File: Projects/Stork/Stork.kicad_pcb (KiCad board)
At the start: 4 copper layers, 200 x 100 mm, 567 parts, among them J1 Conn_01x05, J10 Conn_01x05, J11 Conn_01x05, J12 Conn_01x05, J13 Conn_01x05, J14 Conn_01x05, J15 Conn_01x05, J16 Conn_01x05, J17 Conn_01x05, J18 Conn_01x05, J19 Conn_01x05, J2 Conn_01x05, J20 Conn_01x05, J21 Conn_01x05, J22 Conn_01x05, J23 Conn_01x05, J24 Conn_01x05, J25 Conn_02x03_Odd_Even, J26 Conn_01x03_Male, J27 Screw_Terminal_01x02, J28 Conn_01x03_Male, J29 Conn_01x03_Male, J3 Conn_01x05, J30 Conn_01x03_Male, J4 Conn_01x05, J5 Conn_01x05, J6 Conn_01x05, J7 Conn_01x05, J8 Conn_01x05, J9 Conn_01x05, U1 AD7991YRJZ-1500RL7, U10 AD8608ARZ-SOIC127P600X175-14N, U11 AD7991YRJZ-1500RL7, U12 AD8608ARZ-SOIC127P600X175-14N, U13 AD7991YRJZ-1500RL7, U14 AD8608ARZ-SOIC127P600X175-14N, U15 AD7991YRJZ-1500RL7, U16 AD8608ARZ-SOIC127P600X175-14N, U17 AD7991YRJZ-1500RL7, U18 AD8608ARZ-SOIC127P600X175-14N, U19 AD7991YRJZ-1500RL7, U2 AD8608ARZ-SOIC127P600X175-14N, U20 AD8608ARZ-SOIC127P600X175-14N, U21 AD7991YRJZ-1500RL7, U22 AD8608ARZ-SOIC127P600X175-14N, U23 AD7991YRJZ-1500RL7, U24 AD8608ARZ-SOIC127P600X175-14N, U25 AD7991YRJZ-1500RL7, U26 AD8608ARZ-SOIC127P600X175-14N, U27 AD7991YRJZ-1500RL7, U28 AD8608ARZ-SOIC127P600X175-14N, U29 AD7991YRJZ-1500RL7, U3 AD7991YRJZ-1500RL7, U30 AD8608ARZ-SOIC127P600X175-14N, U31 AD7991YRJZ-1500RL7, U32 AD8608ARZ-SOIC127P600X175-14N, U33 Digilent-CoraZ7, U34 AD7991YRJZ-1500RL7, U35 AD8608ARZ-SOIC127P600X175-14N, U36 AD7991YRJZ-1500RL7, U37 AD8608ARZ-SOIC127P600X175-14N, U38 AD7991YRJZ-1500RL7, U39 AD8608ARZ-SOIC127P600X175-14N, U4 AD8608ARZ-SOIC127P600X175-14N, U40 AD7991YRJZ-1500RL7, U41 AD8608ARZ-SOIC127P600X175-14N, U42 AD7991YRJZ-1500RL7, U43 AD8608ARZ-SOIC127P600X175-14N, U44 AD7991YRJZ-1500RL7, U45 AD8608ARZ-SOIC127P600X175-14N, U46 AD7991YRJZ-1500RL7, U47 AD8608ARZ-SOIC127P600X175-14N, U48 AD7991YRJZ-1500RL7, U49 AD8608ARZ-SOIC127P600X175-14N, U5 AD7991YRJZ-1500RL7, U50 TPS79330-EP, U51 TPS73150DBV, U6 AD8608ARZ-SOIC127P600X175-14N, U7 AD7991YRJZ-1500RL7, U8 AD8608ARZ-SOIC127P600X175-14N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

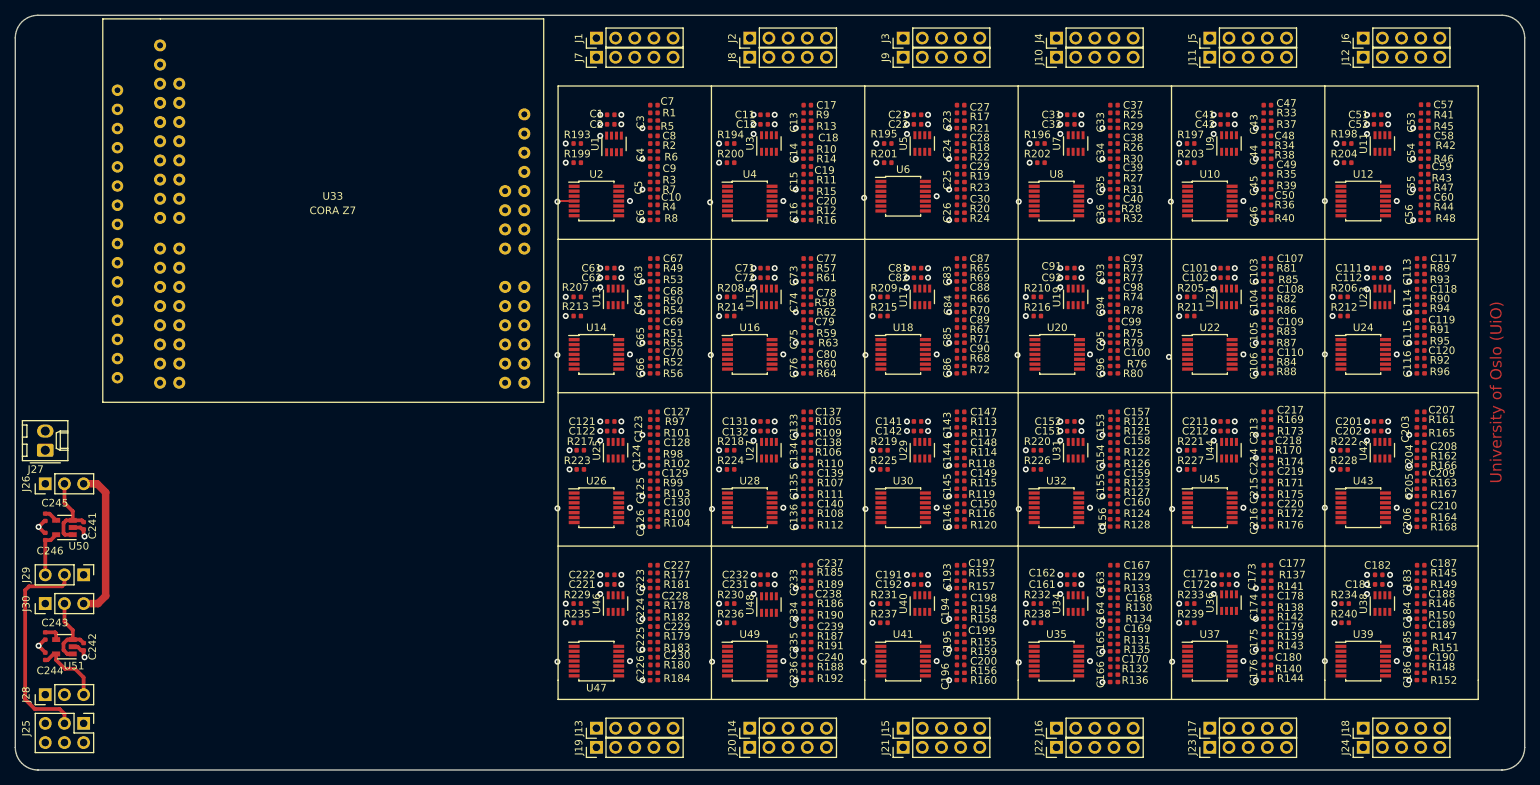
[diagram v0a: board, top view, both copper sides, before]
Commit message: changed position of cora z7 to be at center with cutout to give headroom for ethernet and powerjack
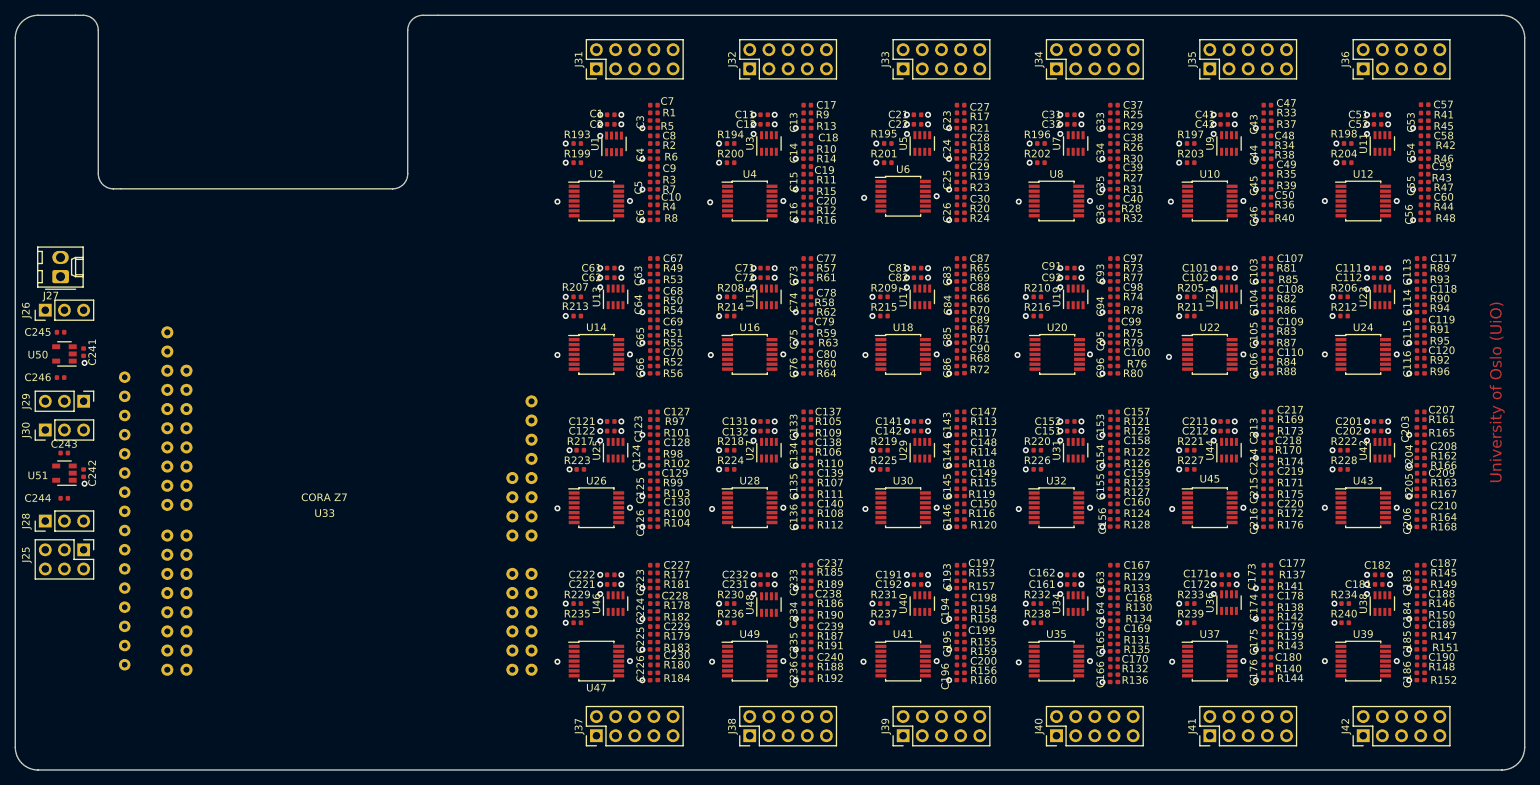
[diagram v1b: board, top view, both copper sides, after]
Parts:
- removed J1, J10, J11, J12, J13, J14, J15, J16, J17, J18, J19, J2, J20, J21, J22, J23, J24, J3, J4, J5, J6, J7, J8, J9: Conn_01x05, Connector_PinHeader_2.54mm:PinHeader_1x05_P2.54mm_Vertical
- added J31: Conn_02x05_Top_Bottom, Connector_PinHeader_2.54mm:PinHeader_2x05_P2.54mm_Vertical, F.Cu at (127.0, 37.1)
- added J32: Conn_02x05_Top_Bottom, Connector_PinHeader_2.54mm:PinHeader_2x05_P2.54mm_Vertical, F.Cu at (147.3, 37.1)
- added J33: Conn_02x05_Top_Bottom, Connector_PinHeader_2.54mm:PinHeader_2x05_P2.54mm_Vertical, F.Cu at (167.6, 37.1)
- added J34: Conn_02x05_Top_Bottom, Connector_PinHeader_2.54mm:PinHeader_2x05_P2.54mm_Vertical, F.Cu at (188.0, 37.1)
- added J35: Conn_02x05_Top_Bottom, Connector_PinHeader_2.54mm:PinHeader_2x05_P2.54mm_Vertical, F.Cu at (208.3, 37.1)
- added J36: Conn_02x05_Top_Bottom, Connector_PinHeader_2.54mm:PinHeader_2x05_P2.54mm_Vertical, F.Cu at (228.6, 37.1)
- added J37: Conn_02x05_Top_Bottom, Connector_PinHeader_2.54mm:PinHeader_2x05_P2.54mm_Vertical, F.Cu at (127.0, 125.5)
- added J38: Conn_02x05_Top_Bottom, Connector_PinHeader_2.54mm:PinHeader_2x05_P2.54mm_Vertical, F.Cu at (147.3, 125.5)
- added J39: Conn_02x05_Top_Bottom, Connector_PinHeader_2.54mm:PinHeader_2x05_P2.54mm_Vertical, F.Cu at (167.6, 125.5)
- added J40: Conn_02x05_Top_Bottom, Connector_PinHeader_2.54mm:PinHeader_2x05_P2.54mm_Vertical, F.Cu at (188.0, 125.5)
- added J41: Conn_02x05_Top_Bottom, Connector_PinHeader_2.54mm:PinHeader_2x05_P2.54mm_Vertical, F.Cu at (208.3, 125.5)
- added J42: Conn_02x05_Top_Bottom, Connector_PinHeader_2.54mm:PinHeader_2x05_P2.54mm_Vertical, F.Cu at (228.6, 125.5)
- U33: footprint footprint:CoraZ7 -> footprint:CoraZ7_stack
- moved U33 49.7 mm to (63.0, 131.0)
- moved C245 24.6 mm to (56.0, 72.0), turned to 0 degrees
- moved C243 24.4 mm to (56.5, 88.0), turned to 0 degrees
- moved J27 23.1 mm to (56.0, 64.6)
- moved C241 23.0 mm to (59.1, 74.6)
- moved C242 23.0 mm to (59.1, 90.7)
- moved J25 23.0 mm to (59.1, 100.8)
- moved J26 23.0 mm to (54.0, 69.1)
- moved J28 23.0 mm to (54.0, 97.0)
- moved J29 23.0 mm to (59.1, 81.1)
- moved J30 23.0 mm to (54.0, 85.0)
- moved U50 23.0 mm to (56.5, 74.9)
- moved U51 23.0 mm to (56.5, 90.7)
- moved C246 21.2 mm to (56.0, 78.0), turned to 0 degrees
- moved C244 21.1 mm to (56.5, 94.0), turned to 0 degrees
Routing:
- net VDD_Filters: track 662.7 -> 0.00 mm, vias 24 -> 13
- net 5V_CoraZ7: track 184.3 -> 0.00 mm
- net V_RAW: track 31.4 -> 0.00 mm
- net 3V3_CoraZ7: track 29.1 -> 0.00 mm, vias 0 -> 2
- net +3V3: track 28.5 -> 0.00 mm, vias 118 -> 123
- net Net-(C241-Pad1): track 10.9 -> 0.00 mm
- net Net-(C242-Pad1): track 10.6 -> 0.00 mm
- net GND: track 10.4 -> 0.00 mm, vias 172 -> 166
- net 5V_Reg: track 9.47 -> 0.00 mm
- net 3V3_Reg: track 6.34 -> 0.00 mm
- net +5V: track 4.86 -> 0.00 mm
- net Net-(C243-Pad1): track 2.32 -> 0.00 mm
- net Net-(C245-Pad1): track 1.81 -> 0.00 mm
- net SDA20: vias 0 -> 1
- net SDA18: vias 0 -> 2
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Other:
- outline, holes or cut-outs redrawn

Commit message: added mounting holes
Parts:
- added REF**: MountingHole_3mm_Pad, MountingHole:MountingHole_3mm_Pad, F.Cu at (55.0, 35.0)
- added REF**: MountingHole_3mm_Pad, MountingHole:MountingHole_3mm_Pad, F.Cu at (245.0, 35.0)
- added REF**: MountingHole_3mm_Pad, MountingHole:MountingHole_3mm_Pad, F.Cu at (245.0, 125.0)
- added REF**: MountingHole_3mm_Pad, MountingHole:MountingHole_3mm_Pad, F.Cu at (55.0, 125.0)
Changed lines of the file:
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@@
     (tracks 312)
     (zones 0)
-    (modules 555)
+    (modules 559)
     (nets 483)
   )
@@
   (layers
     (0 F.Cu signal)
-    (1 In1.Cu signal hide)
+    (1 In1.Cu signal)
     (2 In2.Cu signal)
     (31 B.Cu signal)
@@
     (add_net V_RAW)
   )
+  (module MountingHole:MountingHole_3mm_Pad (layer F.Cu)
+    (at 55 35)
+    (descr "Mounting Hole 3mm")
+    (tags "mounting hole 3mm")
+    (attr virtual)
+    (fp_text reference REF** (at 0 -4) (layer F.SilkS) hide
+      (effects (font (size 1 1) (thickness 0.15)))
+    )
+    (fp_text value MountingHole_3mm_Pad (at 0 4) (layer F.Fab)
+      (effects (font (size 1 1) (thickness 0.15)))
+    )
+    (fp_circle (center 0 0) (end 3.25 0) (layer F.CrtYd) (width 0.05))
+    (fp_circle (center 0 0) (end 3 0) (layer Cmts.User) (width 0.15))
+    (fp_text user %R (at 0.3 0) (layer F.Fab)
+      (effects (font (size 1 1) (thickness 0.15)))
+    )
+    (pad 1 thru_hole circle (at 0 0) (size 6 6) (drill 3) (layers *.Cu *.Mask))
+  )
+  (module MountingHole:MountingHole_3mm_Pad (layer F.Cu)
+    (at 245 35)
+    (descr "Mounting Hole 3mm")
+    (tags "mounting hole 3mm")
+    (attr virtual)
+    (fp_text reference REF** (at 0 -4) (layer F.SilkS) hide
+      (effects (font (size 1 1) (thickness 0.15)))
+    )
+    (fp_text value MountingHole_3mm_Pad (at 0 4) (layer F.Fab)
+      (effects (font (size 1 1) (thickness 0.15)))
+    )
+    (fp_circle (center 0 0) (end 3.25 0) (layer F.CrtYd) (width 0.05))
+    (fp_circle (center 0 0) (end 3 0) (layer Cmts.User) (width 0.15))
+    (fp_text user %R (at 0.3 0) (layer F.Fab)
+      (effects (font (size 1 1) (thickness 0.15)))
+    )
+    (pad 1 thru_hole circle (at 0 0) (size 6 6) (drill 3) (layers *.Cu *.Mask))
+  )
+  (module MountingHole:MountingHole_3mm_Pad (layer F.Cu)
+    (at 245 125)
+    (descr "Mounting Hole 3mm")
+    (tags "mounting hole 3mm")
+    (attr virtual)
+    (fp_text reference REF** (at 0 -4) (layer F.SilkS) hide
+      (effects (font (size 1 1) (thickness 0.15)))
+    )
+    (fp_text value MountingHole_3mm_Pad (at 0 4) (layer F.Fab)
+      (effects (font (size 1 1) (thickness 0.15)))
+    )
+    (fp_circle (center 0 0) (end 3.25 0) (layer F.CrtYd) (width 0.05))
+    (fp_circle (center 0 0) (end 3 0) (layer Cmts.User) (width 0.15))
+    (fp_text user %R (at 0.3 0) (layer F.Fab)
+      (effects (font (size 1 1) (thickness 0.15)))
+    )
+    (pad 1 thru_hole circle (at 0 0) (size 6 6) (drill 3) (layers *.Cu *.Mask))
+  )
+  (module MountingHole:MountingHole_3mm_Pad (layer F.Cu)
+    (at 55 125)
+    (descr "Mounting Hole 3mm")
+    (tags "mounting hole 3mm")
+    (attr virtual)
+    (fp_text reference REF** (at 1 -5) (layer F.SilkS) hide
+      (effects (font (size 1 1) (thickness 0.15)))
+    )
+    (fp_text value MountingHole_3mm_Pad (at 0 4) (layer F.Fab)
+      (effects (font (size 1 1) (thickness 0.15)))
+    )
+    (fp_circle (center 0 0) (end 3.25 0) (layer F.CrtYd) (width 0.05))
+    (fp_circle (center 0 0) (end 3 0) (layer Cmts.User) (width 0.15))
+    (fp_text user %R (at 0.3 0) (layer F.Fab)
+      (effects (font (size 1 1) (thickness 0.15)))
+    )
+    (pad 1 thru_hole circle (at 0 0) (size 6 6) (drill 3) (layers *.Cu *.Mask))
+  )
   (module Capacitor_SMD:C_0402_1005Metric (layer F.Cu)

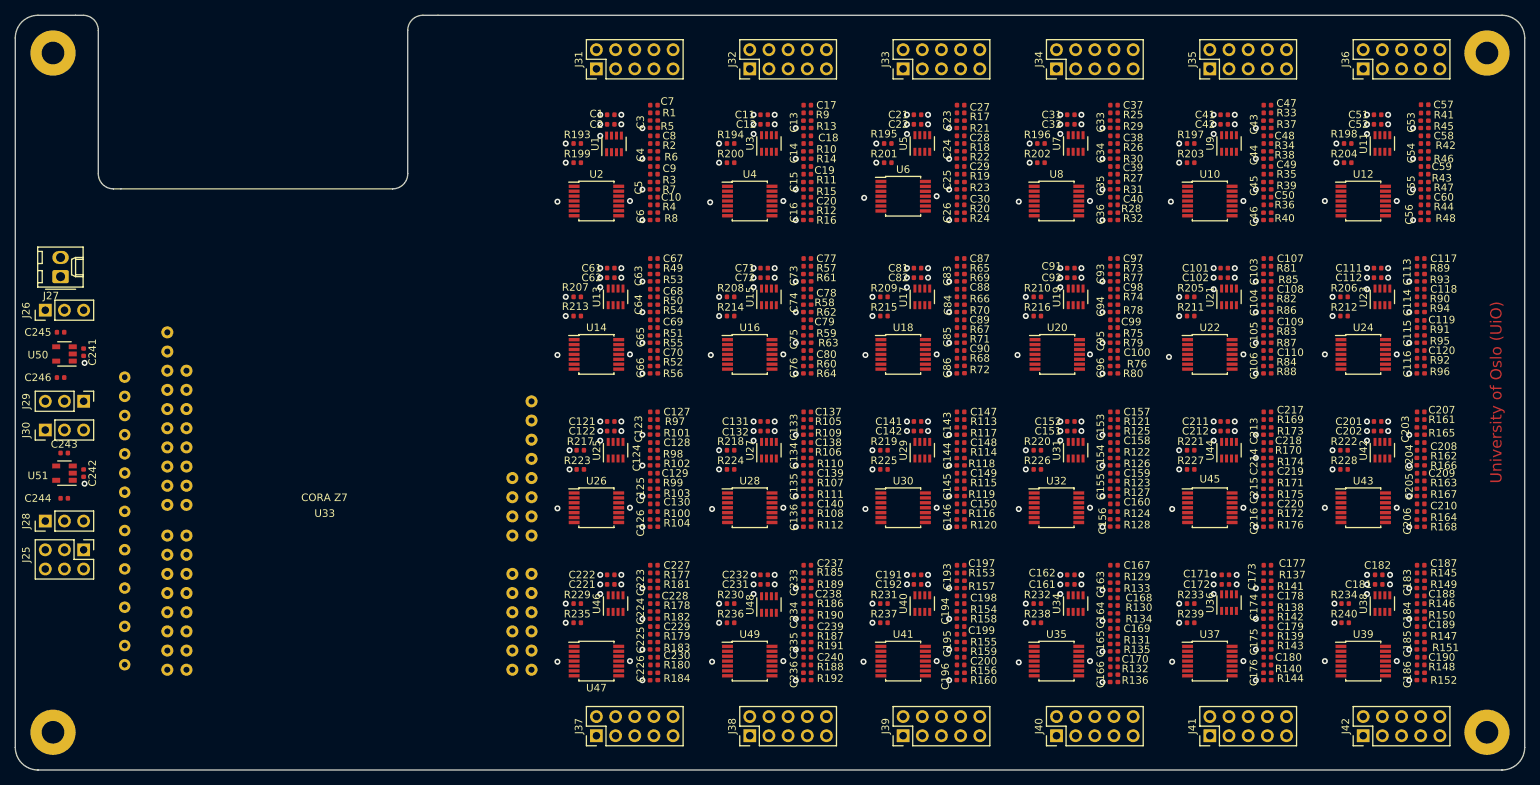
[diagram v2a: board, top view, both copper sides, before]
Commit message: added mounting hole in schematic and corresponding footprint on layout
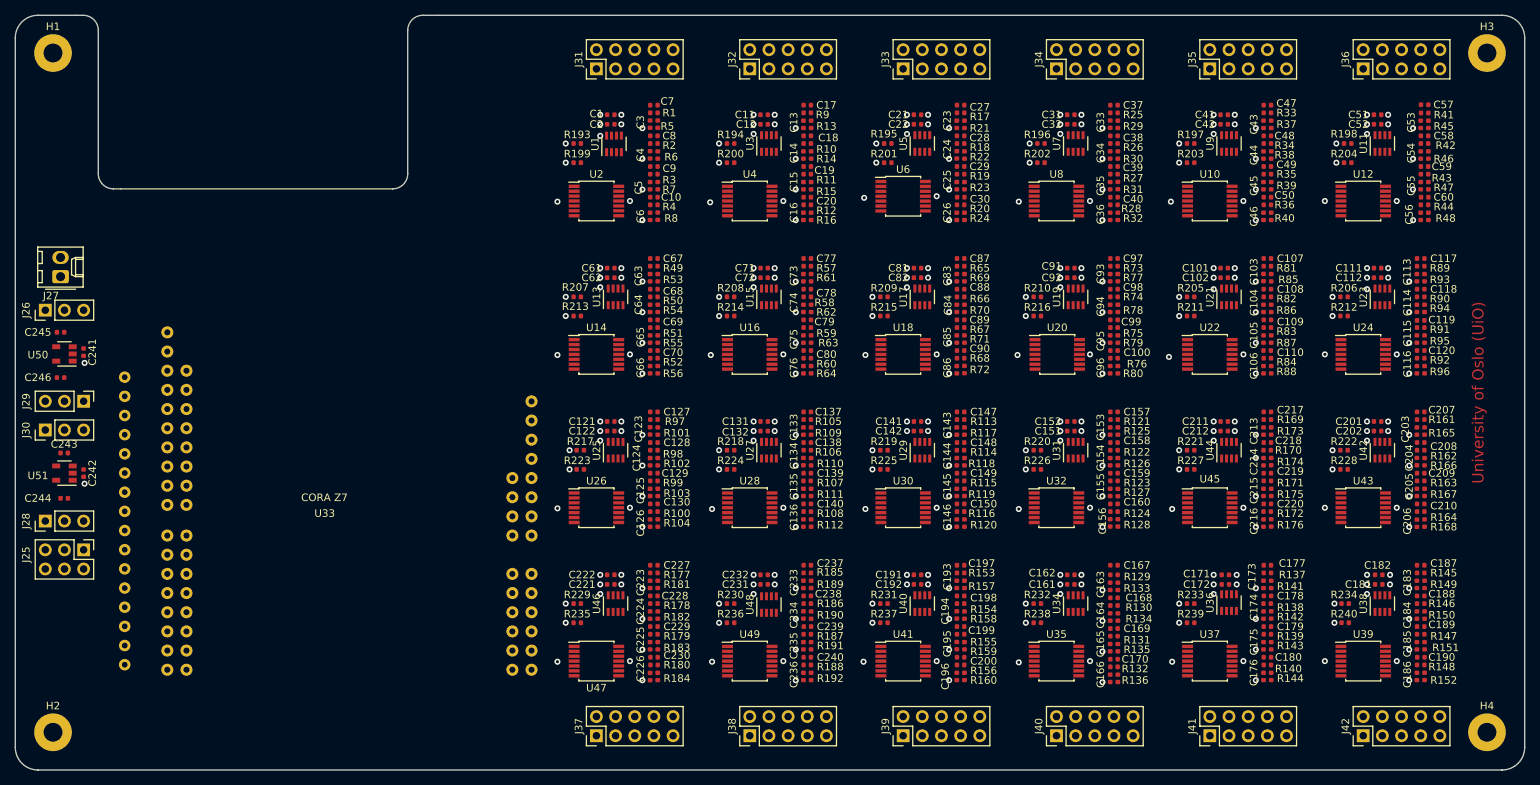
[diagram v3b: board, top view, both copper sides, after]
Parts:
- removed REF** (x4): MountingHole_3mm_Pad, MountingHole:MountingHole_3mm_Pad
- added H1: MountingHole, MountingHole:MountingHole_2.5mm_Pad, F.Cu at (55.0, 35.0)
- added H2: MountingHole, MountingHole:MountingHole_2.5mm_Pad, F.Cu at (55.0, 125.0)
- added H3: MountingHole, MountingHole:MountingHole_2.5mm_Pad, F.Cu at (245.0, 35.0)
- added H4: MountingHole, MountingHole:MountingHole_2.5mm_Pad, F.Cu at (245.0, 125.0)
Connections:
- J31 pad 1: Net-(J31-Pad1) -> GND
- J31 pad 2: Net-(J31-Pad2) -> GND
- J32 pad 1: Net-(J32-Pad1) -> GND
- J32 pad 2: Net-(J32-Pad2) -> GND
- J34 pad 1: Net-(J34-Pad1) -> GND
- J34 pad 2: Net-(J34-Pad2) -> GND
- J35 pad 1: Net-(J35-Pad1) -> GND
- J35 pad 2: Net-(J35-Pad2) -> GND
- J36 pad 1: Net-(J36-Pad1) -> GND
- J36 pad 2: Net-(J36-Pad2) -> GND
- J37 pad 1: Net-(J37-Pad1) -> GND
- J37 pad 2: Net-(J37-Pad2) -> GND
- J38 pad 1: Net-(J38-Pad1) -> GND
- J38 pad 2: Net-(J38-Pad2) -> GND
- J40 pad 1: Net-(J40-Pad1) -> GND
- J40 pad 2: Net-(J40-Pad2) -> GND
- J41 pad 1: Net-(J41-Pad1) -> GND
- J41 pad 2: Net-(J41-Pad2) -> GND
- J42 pad 1: Net-(J42-Pad1) -> GND
- J42 pad 2: Net-(J42-Pad2) -> GND

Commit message: updated net class
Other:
- net class Power added: clearance 0.4, trace_width 0.5, via_dia 0.8, via_drill 0.4
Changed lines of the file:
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@@
     (uvia_dia 0.3)
     (uvia_drill 0.1)
-    (add_net +3V3)
-    (add_net +5V)
-    (add_net 3V3_CoraZ7)
-    (add_net 3V3_Reg)
-    (add_net 5V_CoraZ7)
-    (add_net 5V_Reg)
-    (add_net GND)
     (add_net "Net-(C10-Pad1)")
     (add_net "Net-(C10-Pad2)")
@@
     (add_net SDA8)
     (add_net SDA9)
-    (add_net VDD_Filters)
-    (add_net VDD_Filters_External)
     (add_net VIN1_0)
     (add_net VIN1_1)
@@
     (add_net VIN4_8)
     (add_net VIN4_9)
+  )
+  (net_class Power ""
+    (clearance 0.4)
+    (trace_width 0.5)
+    (via_dia 0.8)
+    (via_drill 0.4)
+    (uvia_dia 0.3)
+    (uvia_drill 0.1)
+    (add_net +3V3)
+    (add_net +5V)
+    (add_net 3V3_CoraZ7)
+    (add_net 3V3_Reg)
+    (add_net 5V_CoraZ7)
+    (add_net 5V_Reg)
+    (add_net GND)
+    (add_net VDD_Filters)
+    (add_net VDD_Filters_External)
     (add_net V_RAW)
   )
@@
       )
     )
-  )
-  (zone (net 0) (net_name "") (layers F&B.Cu) (hatch edge 0.508)
-    (connect_pads (clearance 0.508))
-    (min_thickness 0.254)
-    (keepout (tracks not_allowed) (vias not_allowed) (copperpour allowed))
-    (fill (arc_segments 32) (thermal_gap 0.508) (thermal_bridge_width 0.508))
-    (polygon
-      (pts
-        (xy 250 130) (xy 50 130) (xy 50 128) (xy 250 128)
-      )
-    )
-  )
-  (zone (net 0) (net_name "") (layers F&B.Cu) (hatch edge 0.508)
-    (connect_pads (clearance 0.508))
-    (min_thickness 0.254)
-    (keepout (tracks not_allowed) (vias not_allowed) (copperpour allowed))
-    (fill (arc_segments 32) (thermal_gap 0.508) (thermal_bridge_width 0.508))
-    (polygon
-      (pts
-        (xy 250 32) (xy 50 32) (xy 50 30) (xy 250 30)
-      )
-    )
-  )
-  (zone (net 0) (net_name "") (layers F&B.Cu) (hatch edge 0.508)
-    (connect_pads (clearance 0.508))
-    (min_thickness 0.254)
-    (keepout (tracks not_allowed) (vias not_allowed) (copperpour allowed))
-    (fill (arc_segments 32) (thermal_gap 0.508) (thermal_bridge_width 0.508))
-    (polygon
-      (pts
-        (xy 52 130) (xy 50 130) (xy 50 30) (xy 52 30)
-      )
-    )
-  )
-  (zone (net 0) (net_name "") (layers F&B.Cu) (hatch edge 0.508)
-    (connect_pads (clearance 0.508))
-    (min_thickness 0.254)
-    (keepout (tracks not_allowed) (vias not_allowed) (copperpour allowed))
-    (fill (arc_segments 32) (thermal_gap 0.508) (thermal_bridge_width 0.508))
-    (polygon
-      (pts
-        (xy 250 130) (xy 248 130) (xy 248 30) (xy 250 30)
-      )
-    )
